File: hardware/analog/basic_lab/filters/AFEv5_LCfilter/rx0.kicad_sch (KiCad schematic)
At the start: 7 parts, among them J5 Connector_Generic_Conn_01x02, J6 Connector_Generic_Conn_01x02

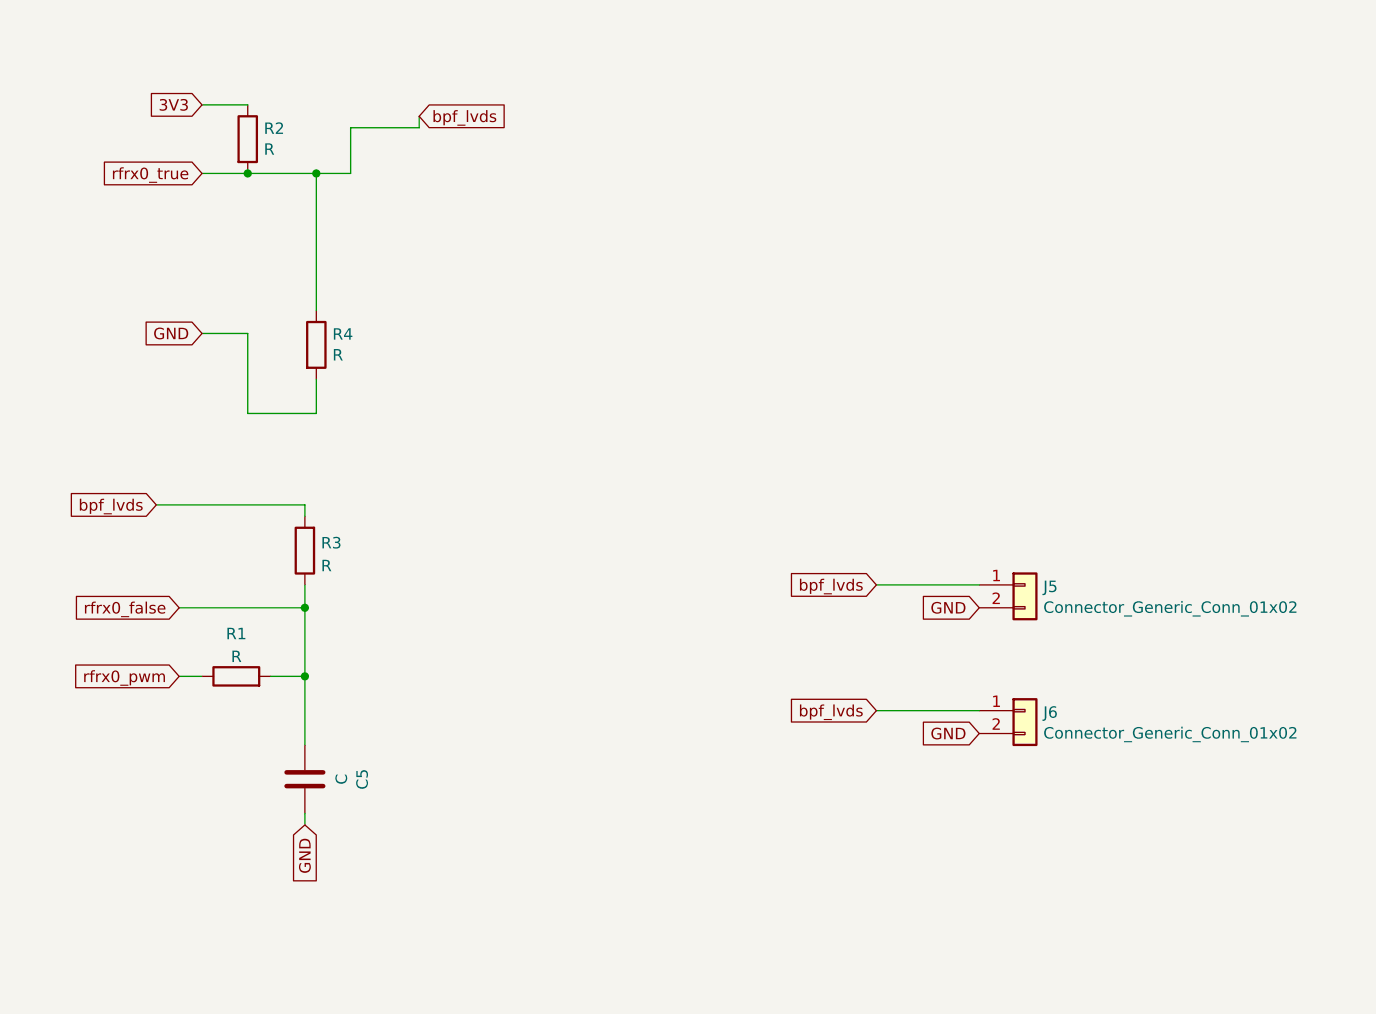
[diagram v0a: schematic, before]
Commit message: started new AFE with central power filters, offset DAC LC RF filter
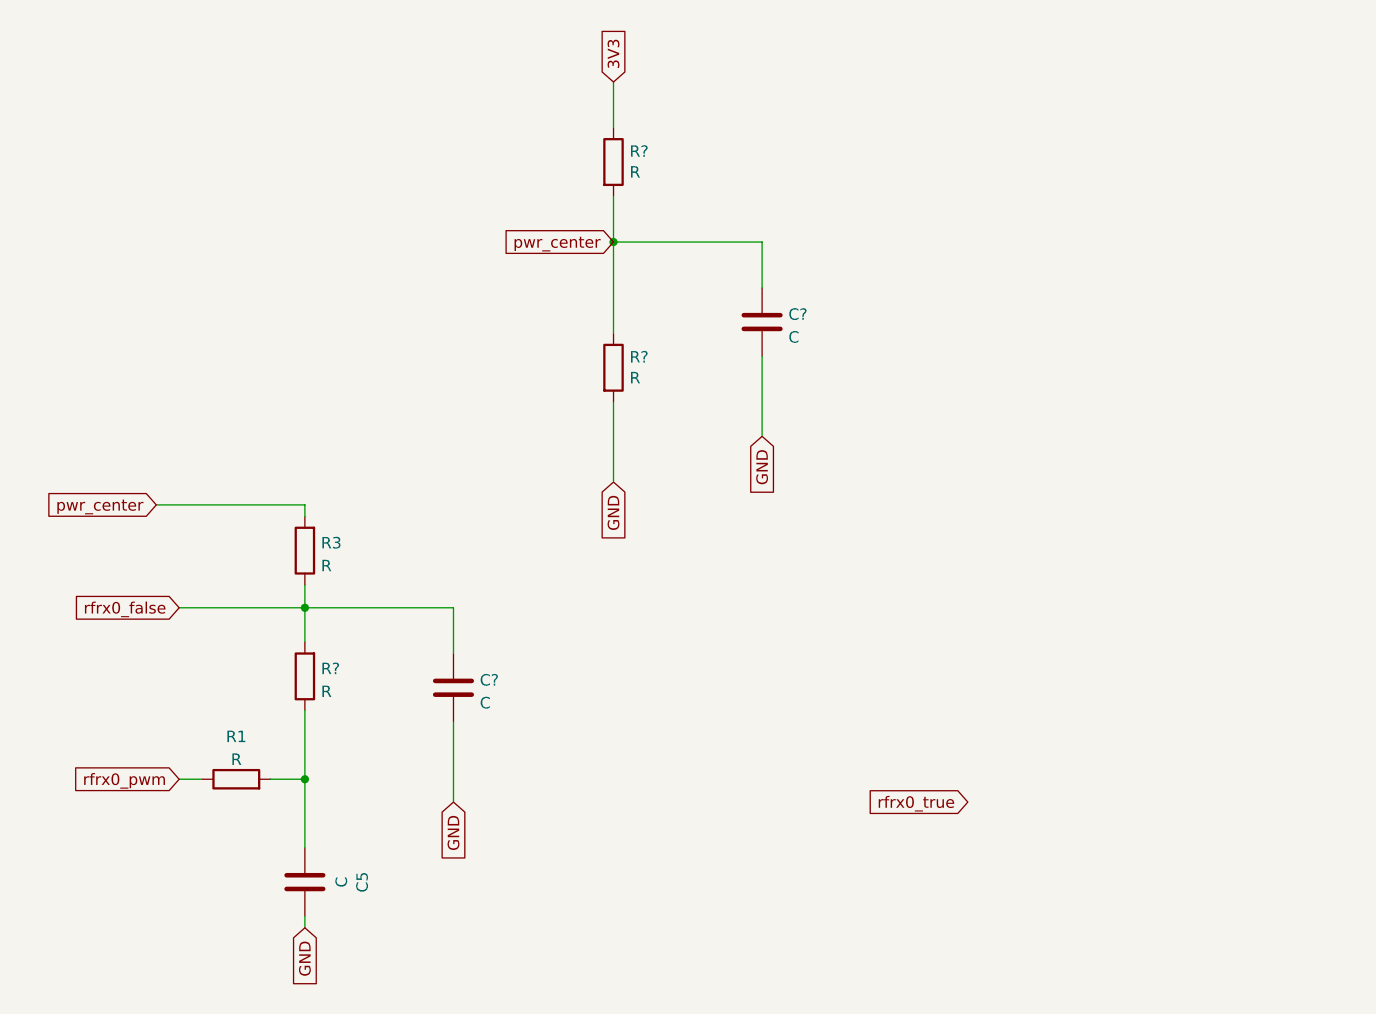
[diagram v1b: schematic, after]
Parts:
- removed J5, J6: Connector_Generic_Conn_01x02, Connector_PinHeader_2.54mm:PinHeader_1x02_P2.54mm_Vertical, symbol bgt:Connector_Generic_Conn_01x02
- removed R2, R4: R, Resistor_SMD:R_1206_3216Metric, symbol Device:R
- added C? (x2): C, symbol Device:C
- added R? (x3): R, Resistor_SMD:R_1206_3216Metric, symbol Device:R
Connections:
- net 3V3: now also R?.1
- net GND: now also C?.2, C?.2, R?.2
- net rfrx0_false: now also C?.1, R?.2; no longer C5.2, R1.2
- net bpf_lvds renamed pwr_center
- net pwr_center: now also C?.1, R?.1, R?.2
- new net: C5.2, R1.2, R?.1
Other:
- moved on the sheet: C5, R1
